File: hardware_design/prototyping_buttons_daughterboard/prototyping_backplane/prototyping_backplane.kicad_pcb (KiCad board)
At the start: 2 copper layers, 57.6 x 83.8 mm, 17 parts, among them J1 BOOSTER_LEFT, J2 BOOSTER_RIGHT, J3 EXP_SPI, SW1 SW_DIP_x01 CUT LEADS, SW2 SW_DIP_x02

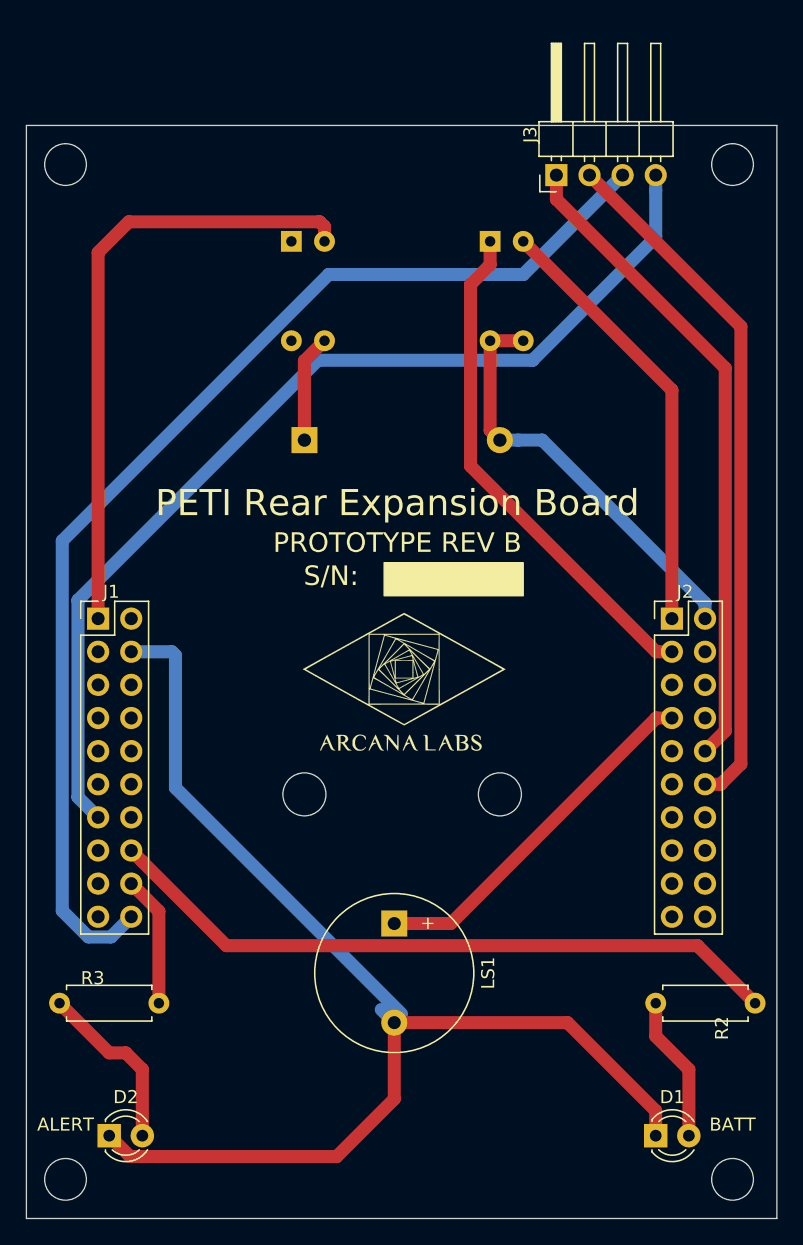
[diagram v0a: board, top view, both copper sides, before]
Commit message: Increment to dev version, add basic hardware functionality for audio, add simple sound test
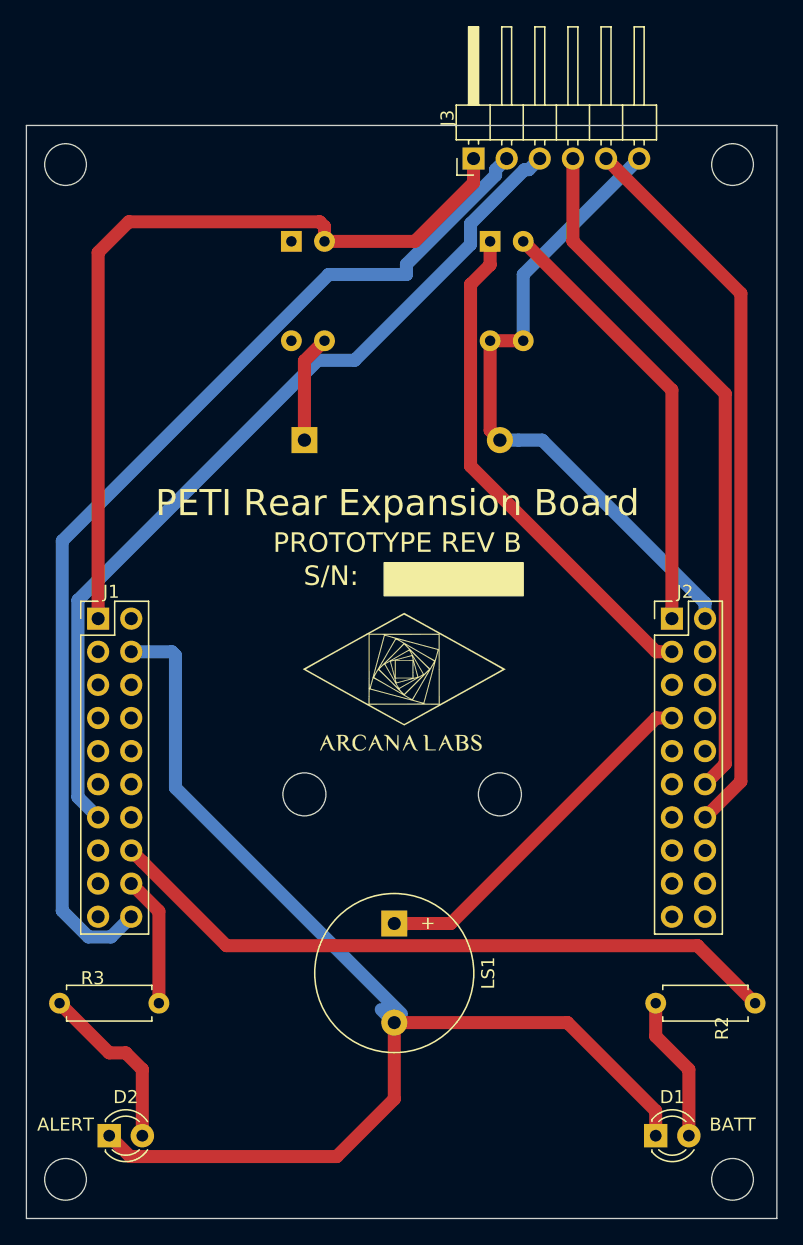
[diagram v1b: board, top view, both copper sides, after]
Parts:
- J3: footprint Connector_PinHeader_2.54mm:PinHeader_1x04_P2.54mm_Horizontal -> Connector_PinHeader_2.54mm:PinHeader_1x06_P2.54mm_Horizontal
- moved J3 6.48 mm to (185.4, 48.3)
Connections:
- J3 pad 1: Net-(J2-Pad10) -> Net-(J1-Pad1)
- J3 pad 2: Net-(J2-Pad12) -> Net-(J1-Pad20)
- J3 pad 3: Net-(J1-Pad20) -> Net-(J1-Pad13)
- J3 pad 4: Net-(J1-Pad13) -> Net-(J2-Pad12)
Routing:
- net Net-(J2-Pad14): track 0.00 -> 55.9 mm
- net Net-(J2-Pad10): track 50.2 -> 0.00 mm
- net Net-(BT1-Pad2): track 32.6 -> 50.2 mm
- net Net-(J1-Pad1): track 47.7 -> 62.8 mm
- net Net-(J1-Pad13): track 77.9 -> 67.7 mm
- net Net-(J1-Pad20): track 89.7 -> 82.1 mm
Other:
- board text added: "3.3v"
- board text added: "CLK"
- board text added: "GND"
- board text added: "MISO"
- board text added: "MOSI"
- board text added: "SEL"
